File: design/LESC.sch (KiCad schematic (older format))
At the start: 0 parts

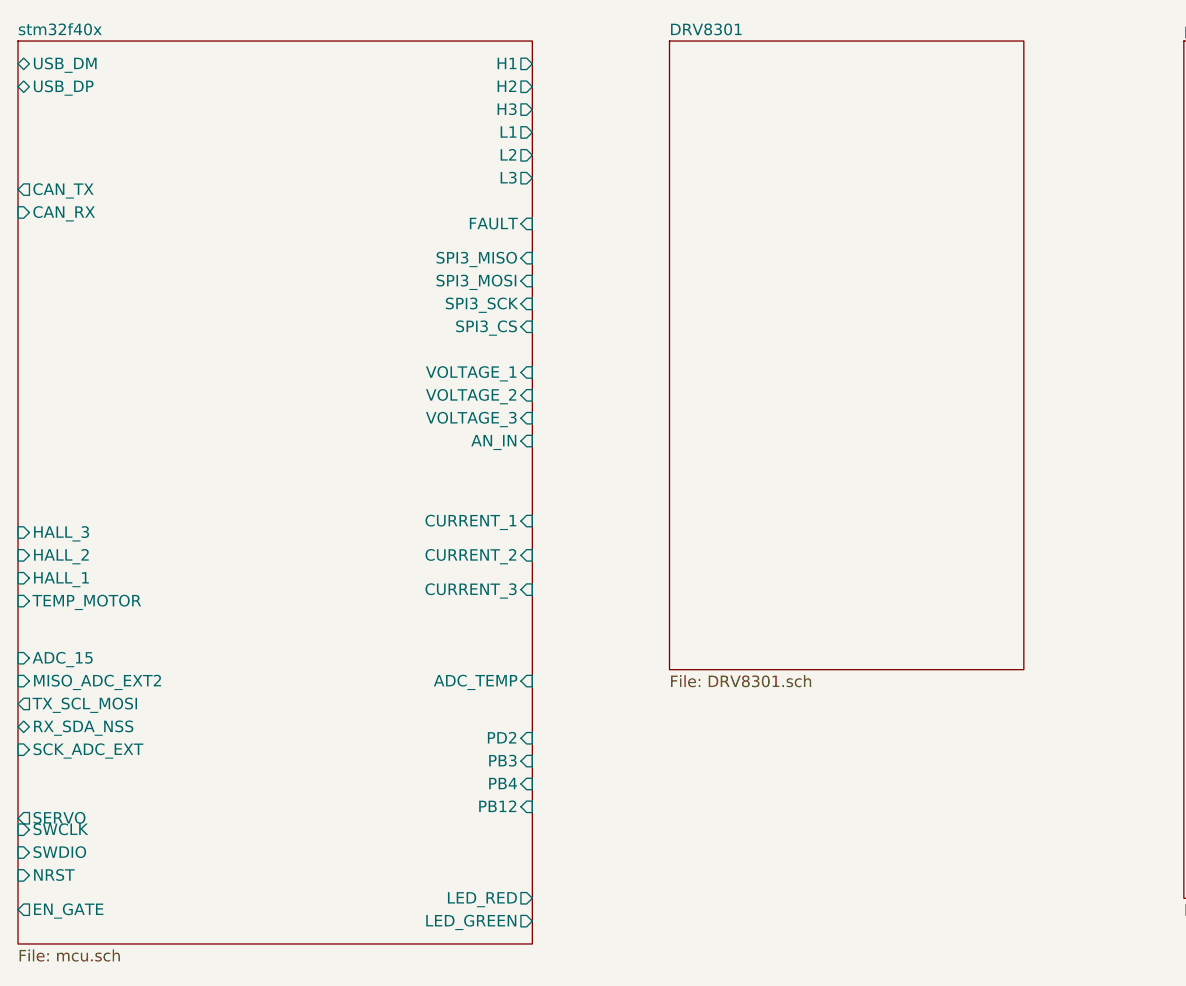
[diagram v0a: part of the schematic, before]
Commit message: done DRV8301
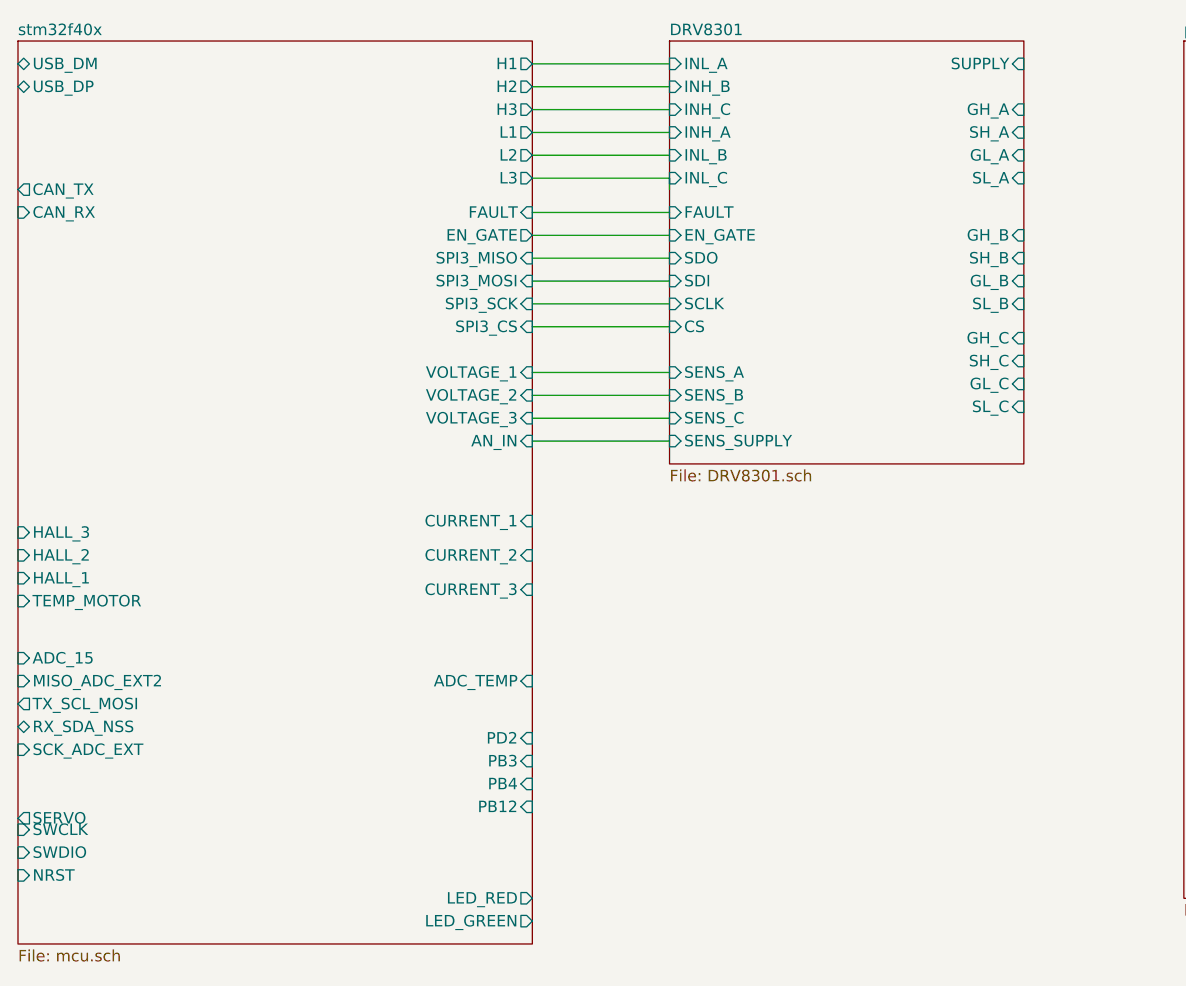
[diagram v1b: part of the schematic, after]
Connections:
- wire segments 0 -> 17
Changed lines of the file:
@@
 F15 "LED_GREEN" O R 6400 5200 50
 F16 "LED_RED" O R 6400 5100 50
-F17 "EN_GATE" O L 4150 5150 50
+F17 "EN_GATE" O R 6400 2200 50
 F18 "SERVO" O L 4150 4750 50
-F19 "FAULT" I R 6400 2150 50
+F19 "FAULT" I R 6400 2100 50
 F20 "CAN_RX" I L 4150 2100 50
 F21 "CAN_TX" O L 4150 2000 50
@@
 $EndSheet
 $Sheet
-S 7000 1350 1550 2750
+S 7000 1350 1550 1850
 U 5AE1478F
 F0 "DRV8301" 50
 F1 "DRV8301.sch" 50
+F2 "FAULT" I L 7000 2100 50
+F3 "CS" I L 7000 2600 50
+F4 "SDI" I L 7000 2400 50
+F5 "SDO" I L 7000 2300 50
+F6 "SCLK" I L 7000 2500 50
+F7 "EN_GATE" I L 7000 2200 50
+F8 "INL_A" I L 7000 1450 50
+F9 "INH_B" I L 7000 1550 50
+F10 "INL_B" I L 7000 1850 50
+F11 "INH_C" I L 7000 1650 50
+F12 "INL_C" I L 7000 1950 50
+F13 "SUPPLY" I R 8550 1450 50
+F14 "GH_A" I R 8550 1650 50
+F15 "GL_A" I R 8550 1850 50
+F16 "SL_A" I R 8550 1950 50
+F17 "GH_B" I R 8550 2200 50
+F18 "GL_B" I R 8550 2400 50
+F19 "SL_B" I R 8550 2500 50
+F20 "GH_C" I R 8550 2650 50
+F21 "GL_C" I R 8550 2850 50
+F22 "SL_C" I R 8550 2950 50
+F23 "SH_A" I R 8550 1750 50
+F24 "SH_B" I R 8550 2300 50
+F25 "SH_C" I R 8550 2750 50
+F26 "SENS_SUPPLY" I L 7000 3100 50
+F27 "SENS_A" I L 7000 2800 50
+F28 "SENS_B" I L 7000 2900 50
+F29 "SENS_C" I L 7000 3000 50
+F30 "INH_A" I L 7000 1750 50
 $EndSheet
 $Sheet
@@
 F1 "power.sch" 50
 $EndSheet
+Wire Wire Line
+	6400 1450 7000 1450
+Wire Wire Line
+	6400 1550 7000 1550
+Wire Wire Line
+	6400 1650 7000 1650
+Wire Wire Line
+	6400 1750 7000 1750
+Wire Wire Line
+	6400 1850 7000 1850
+Wire Wire Line
+	6400 1950 7000 1950
+Wire Wire Line
+	7000 1950 7000 2000
+Wire Wire Line
+	6400 2100 7000 2100
+Wire Wire Line
+	6400 2200 7000 2200
+Wire Wire Line
+	6400 2300 7000 2300
+Wire Wire Line
+	6400 2400 7000 2400
+Wire Wire Line
+	6400 2500 7000 2500
+Wire Wire Line
+	6400 2600 7000 2600
+Wire Wire Line
+	6400 2800 7000 2800
+Wire Wire Line
+	6400 2900 7000 2900
+Wire Wire Line
+	6400 3000 7000 3000
+Wire Wire Line
+	6400 3100 7000 3100
 $EndSCHEMATC

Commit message: finish power and can schematic but many components librariy has error
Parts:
- added J?: USB_OTG, symbol Connector:USB_OTG
- added R? (x3): R, symbol Device:R
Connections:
- net labels added: +5V, GND, SUPPLY, VCC
- wire segments 17 -> 47

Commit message: schematic almost finish
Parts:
- added C? (x2): C, symbol Device:C
- added D?: BLUE, symbol Device:LED
- added D?: RED, symbol Device:LED
- added D?: GREEN, symbol Device:LED
- added J?: CAN, symbol Connector_Generic:Conn_01x04
- added J?: HALL_ENC, symbol Connector_Generic:Conn_01x06
- added J?: COMM, symbol Connector_Generic:Conn_01x08
- added J?: SERVO, symbol Connector_Generic:Conn_01x03
- added J?: SWD, symbol Connector_Generic:Conn_01x05
- added R? (x8): R, symbol Device:R
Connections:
- wire segments 47 -> 112
- no-connect marks 0 -> 2
